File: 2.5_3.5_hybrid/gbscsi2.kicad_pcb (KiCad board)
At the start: 4 copper layers, 69.5 x 93.5 mm, 113 parts, among them J1 Conn_01x02, J2 TF003, J4 Conn_01x04, J5 SCSI_50-2P_2mm, J6 SCSI_50P_2.54mm, Q1 AO3401A, Q10 AO3401A, Q11 AO3401A, Q12 AO3401A, Q13 AO3401A, Q14 AO3401A, Q15 AO3401A, Q16 AO3401A, Q17 AO3401A, Q18 AO3401A, Q2 AO3401A, Q3 AO3401A, Q4 AO3401A, Q5 AO3401A, Q6 AO3401A, Q7 AO3401A, Q8 AO3401A, Q9 AO3401A, SW1 SW_DIP_x03, U1 Pico W, U2 74LVT245, U3 74LVT245, U4 74AHCT1G125, U5 74LVT125, U6 74LVT125, U7 AZ1117-2.85, U8 AP62250WU

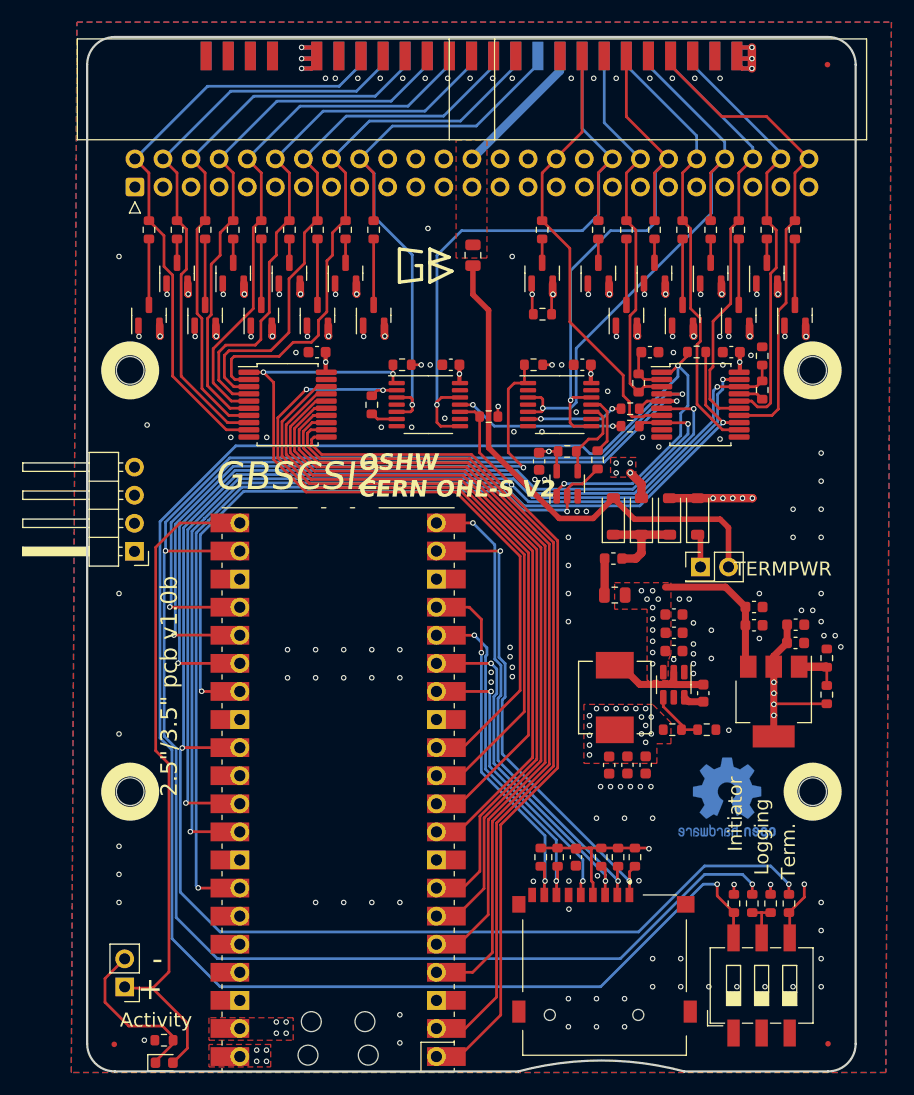
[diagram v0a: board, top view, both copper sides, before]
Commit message: Corrected wrong keying on 2.5" connector
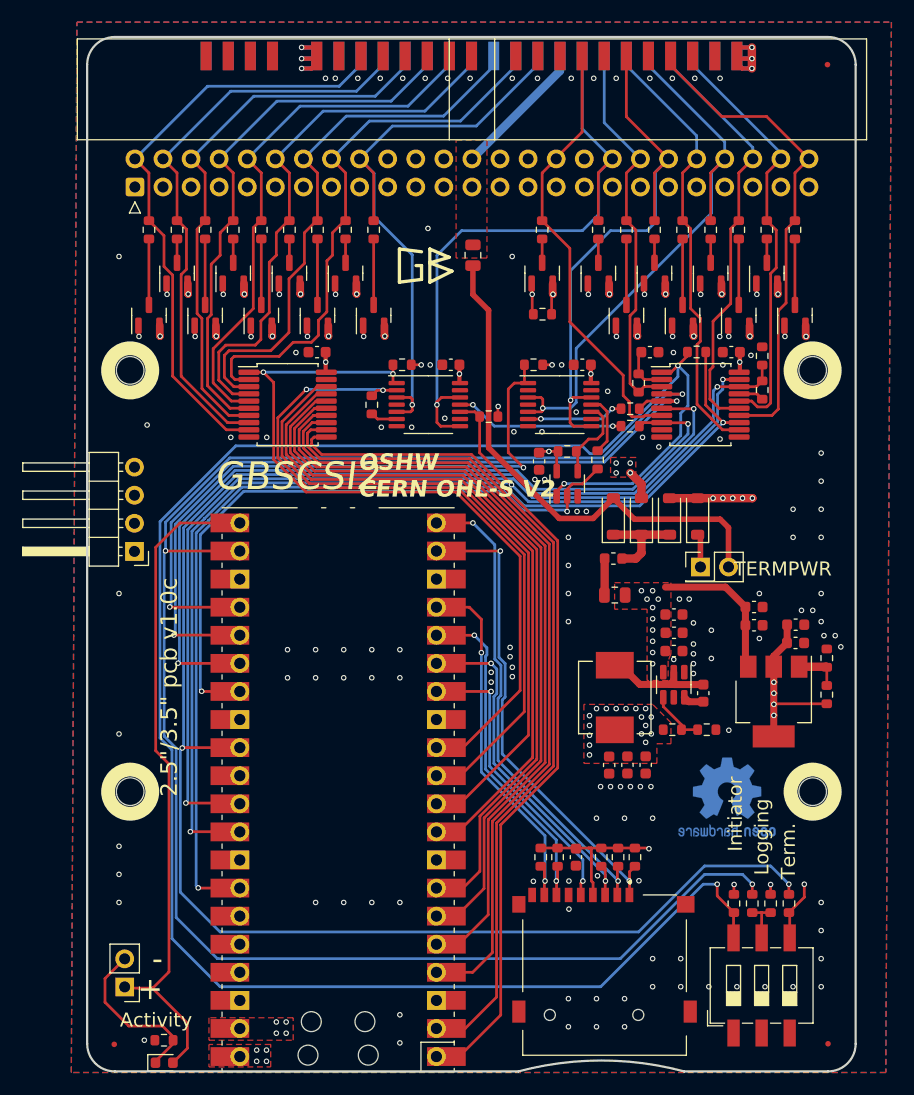
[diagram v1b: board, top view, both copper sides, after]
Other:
- board text added: "2.5{dblquote}/3.5{dblquote} pcb v1.0c"
- board text removed: "2.5{dblquote}/3.5{dblquote} pcb v1.0b"

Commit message: Changed diodes in BoM, minor corrections to PCB, documentation
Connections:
- J5 pad 21: (no net) -> GND
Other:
- board text added: "2.5{dblquote}/3.5{dblquote} pcb v1.0d"
- board text removed: "2.5{dblquote}/3.5{dblquote} pcb v1.0c"

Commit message: Cleaning up, updating docs
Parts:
- C1: value 100nF -> 10uF
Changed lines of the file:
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@@
     (descr "Capacitor SMD 0603 (1608 Metric), square (rectangular) end terminal, IPC_7351 nominal, (Body size source: IPC-SM-782 page 76, https://www.pcb-3d.com/wordpress/wp-content/uploads/ipc-sm-782a_amendment_1_and_2.pdf), generated with kicad-footprint-generator")
     (tags "capacitor")
-    (property "LCSC" "C14663")
+    (property "LCSC" "C96446")
     (property "Sheetfile" "gbscsi2.kicad_sch")
     (property "Sheetname" "")
@@
         (effects (font (size 1 1) (thickness 0.15)))
     )
-    (fp_text value "100nF" (at 0 1.43 -270) (layer "F.Fab")
+    (fp_text value "10uF" (at 0 1.43 -270) (layer "F.Fab")
         (effects (font (size 1 1) (thickness 0.15)))
     )
